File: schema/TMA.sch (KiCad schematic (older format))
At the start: 24 parts, among them U1 BMP280, U2 BMI160

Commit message: Remove pull-down for SPDT, update symbols.
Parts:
- removed R?: 10k, symbol Device:R_Small
- gave numbers to parts that had none: 21

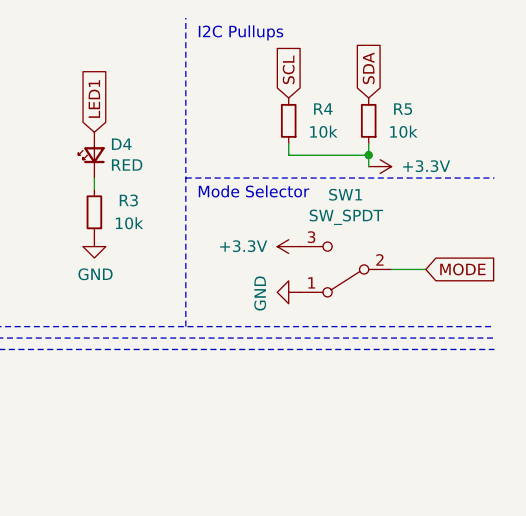
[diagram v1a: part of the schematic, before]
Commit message: Important alignment issues.
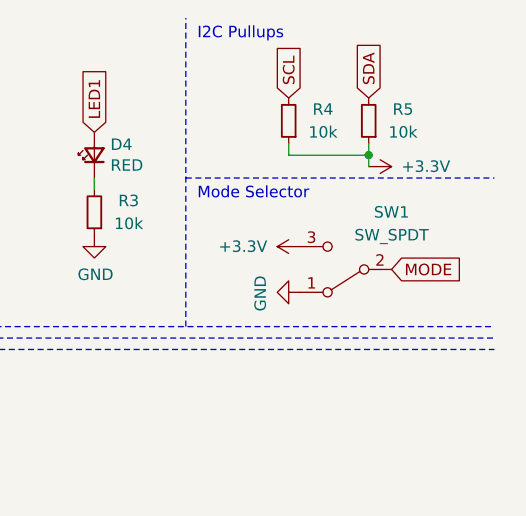
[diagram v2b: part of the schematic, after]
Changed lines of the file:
@@
 U 1 1 60789BF3
 P 10550 1600
-F 0 "SW1" H 10550 1275 50  0000 C CNN
-F 1 "SW_SPDT" H 10550 1366 50  0000 C CNN
+F 0 "SW1" H 10350 1350 50  0000 C CNN
+F 1 "SW_SPDT" H 10350 1450 50  0000 C CNN
 F 2 "" H 10550 1600 50  0001 C CNN
 F 3 "~" H 10550 1600 50  0001 C CNN
@@
 	-1   0    0    1
 $EndComp
-Text GLabel 10900 1600 2    50   Input ~ 0
+Text GLabel 10750 1600 2    50   Input ~ 0
 MODE
 $Comp
@@
 Text GLabel 3950 3100 0    50   Input ~ 0
 MODE
-Wire Wire Line
-	10750 1600 10900 1600
 $EndSCHEMATC
